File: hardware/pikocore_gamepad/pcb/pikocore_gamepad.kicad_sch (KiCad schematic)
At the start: 91 parts, among them J1 PHONES, J2 MIDI OUT, J3 MIDI IN, J4 ST7789_240x240, J5 SPEAKER 8R, J6 microSD, J7 EXP, SW1 DPAD_UP, SW10 BTN_R, SW11 BTN_START, SW12 BTN_SELECT, SW13 NAV1, SW14 NAV2, SW15 PWR, SW2 DPAD_DOWN, SW3 DPAD_LEFT, SW4 DPAD_RIGHT, SW5 BTN_X, SW6 BTN_Y, SW7 BTN_A, SW8 BTN_B, SW9 BTN_L, U1 RP2350-Plus-16MB, U10 PCF8574MT, U11 PCF8574MT, U12 PCF8574MT, U2 TPS61023DRLR, U3 NJM4556AD, U4 PAM8302A, U5 PCM5102APWR, U6 H11L1

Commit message: hw: pikocore_gamepad schematic — checks green, ERC clean
Regenerates the schematic (gen_sch.py), exports the netlist, generates the
placement-only PCB (gen_pcb.py), runs checks/run_all.py and kicad-cli sch erc
as end-to-end verification for the pikocore_gamepad PCB fork.

- checks/run_all.py: G-5 (dup refs), G-4 (pinmap vs firmware, 23/23), G-2
  (netlist match, 226/226), placement (no overlaps) all pass. G-0 still
  reports the 7 pre-existing provisional constants + 4 provisional
  footprints inherited from GAMESETUP (TPS61023/JACK_AUDIO pinouts,
  BOOST_*, BTN_FP/BTN_RA_FP/OPAMP_FP/JACK_FP, LCD_PIN_ROW_Y/LCD_HOLE_INSET,
  BOARD_W/BOARD_H) — expected, not resolved by this plan.
- kicad-cli sch erc: 0 errors, 65 warnings. 3 are the expected dangling
  EXP_GP26/27/28 labels. The other 62 are lib_symbol_issues warnings caused
  by a pre-existing mismatch between sym-lib-table's unrenamed 'gamesetup'
  nickname and gen_sch.py's PROJECT="pikocore_gamepad" lib_id prefix — see
  gen_sch.py's own comment referencing a not-yet-existing 'Task 8' to fix
  sym-lib-table. Flagged for follow-up, not fixed here (out of scope).

logs/erc.log is force-added since pcb/.gitignore's 'logs/*' rule would
otherwise exclude it, per this task's explicit instruction to commit it as
evidence. kicad_pcb/.net are committed to match GAMESETUP's own convention
of tracking these (verified via git ls-files in C:/midigame/GAMESETUP).

Co-Authored-By: Claude Sonnet 5 <noreply@anthropic.com>
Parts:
- removed C1, C10, C11, C13, C15, C2, C20, C27, C29, C3, C30, C7: 100nF, Capacitor_SMD:C_0603_1608Metric, symbol gamesetup:C
- removed C12, C14, C16, C28, C31: 10uF, Capacitor_SMD:CP_Elec_6.3x5.4, symbol gamesetup:CP
- removed C17, C18: 2n2, Capacitor_SMD:C_0603_1608Metric, symbol gamesetup:C
- removed C19, C6: 100uF, Capacitor_SMD:CP_Elec_6.3x5.4, symbol gamesetup:CP
- removed C21, C22, C25, C26: 1uF, Capacitor_SMD:C_0603_1608Metric, symbol gamesetup:C
- removed C23, C24: 470uF, Capacitor_SMD:CP_Elec_6.3x5.4, symbol gamesetup:CP
- removed C4: 10uF, Capacitor_SMD:C_0603_1608Metric, symbol gamesetup:C
- removed C5: 22uF, Capacitor_SMD:C_0603_1608Metric, symbol gamesetup:C
- removed C8, C9: 2u2, Capacitor_SMD:C_0603_1608Metric, symbol gamesetup:C
- removed D1: 1N4148W, Diode_SMD:D_SOD-123, symbol gamesetup:D
- removed J1: PHONES, Connector_PinHeader_2.54mm:PinHeader_1x04_P2.54mm_Vertical, symbol gamesetup:JACK_AUDIO
- removed J2: MIDI OUT, Connector_PinHeader_2.54mm:PinHeader_1x03_P2.54mm_Vertical, symbol gamesetup:JACK_TRS
- removed J3: MIDI IN, Connector_PinHeader_2.54mm:PinHeader_1x03_P2.54mm_Vertical, symbol gamesetup:JACK_TRS
- removed J5: SPEAKER 8R, Connector_JST:JST_PH_B2B-PH-K_1x02_P2.00mm_Vertical, symbol gamesetup:Conn_01x02
- removed J6: microSD, Connector_PinHeader_2.54mm:PinHeader_1x08_P2.54mm_Vertical, symbol gamesetup:MICROSD
- removed J7: EXP, Connector_PinHeader_2.54mm:PinHeader_1x09_P2.54mm_Vertical, symbol gamesetup:Conn_01x09
- removed L1, L2: 2u2, Inductor_SMD:L_1210_3225Metric, symbol gamesetup:L
- removed R1, R2: 4.7k, Resistor_SMD:R_0603_1608Metric, symbol gamesetup:R
- removed R10, R12, R14, R15, R16, R17, R22, R23, R24, R3, R9: 10k, Resistor_SMD:R_0603_1608Metric, symbol gamesetup:R
- removed R11, R13: 20k, Resistor_SMD:R_0603_1608Metric, symbol gamesetup:R
- removed R18, R19: 33R, Resistor_SMD:R_0603_1608Metric, symbol gamesetup:R
- removed R20: 220R, Resistor_SMD:R_0603_1608Metric, symbol gamesetup:R
- removed R21: 1k, Resistor_SMD:R_0603_1608Metric, symbol gamesetup:R
- removed R4: 1M, Resistor_SMD:R_0603_1608Metric, symbol gamesetup:R
- removed R5: 200k, Resistor_SMD:R_0603_1608Metric, symbol gamesetup:R
- removed R6: 100k, Resistor_SMD:R_0603_1608Metric, symbol gamesetup:R
- removed R7, R8: 470R, Resistor_SMD:R_0603_1608Metric, symbol gamesetup:R
- removed SW1: DPAD_UP, gamesetup_lcsc:SW-TH_4P-L4.5-W4.5-P3.00-LS5.5, symbol gamesetup:SW_Push
- removed SW11: BTN_START, gamesetup_lcsc:SW-TH_4P-L4.5-W4.5-P3.00-LS5.5, symbol gamesetup:SW_Push
- removed SW12: BTN_SELECT, gamesetup_lcsc:SW-TH_4P-L4.5-W4.5-P3.00-LS5.5, symbol gamesetup:SW_Push
- removed SW14: NAV2, gamesetup_lcsc:SW-TH_WS-1004-ARL10026, symbol gamesetup:NAV_WS1004
- removed SW15: PWR, gamesetup_lcsc:SW-TH_SK12D07VG3, symbol gamesetup:SK12D07
- removed SW3: DPAD_LEFT, gamesetup_lcsc:SW-TH_4P-L4.5-W4.5-P3.00-LS5.5, symbol gamesetup:SW_Push
- removed SW4: DPAD_RIGHT, gamesetup_lcsc:SW-TH_4P-L4.5-W4.5-P3.00-LS5.5, symbol gamesetup:SW_Push
- removed SW6: BTN_Y, gamesetup_lcsc:SW-TH_4P-L4.5-W4.5-P3.00-LS5.5, symbol gamesetup:SW_Push
- removed SW7: BTN_A, gamesetup_lcsc:SW-TH_4P-L4.5-W4.5-P3.00-LS5.5, symbol gamesetup:SW_Push
- removed SW8: BTN_B, gamesetup_lcsc:SW-TH_4P-L4.5-W4.5-P3.00-LS5.5, symbol gamesetup:SW_Push
- removed TP2: SPARE2, TestPoint:TestPoint_Pad_D1.5mm, symbol gamesetup:TP
- removed U11, U12: PCF8574MT, Package_SO:TSSOP-16_4.4x5mm_P0.65mm, symbol gamesetup:PCF8574
- removed U2: TPS61023DRLR, Package_TO_SOT_SMD:SOT-563, symbol gamesetup:TPS61023
- removed U3: NJM4556AD, Package_SO:SOIC-8_3.9x4.9mm_P1.27mm, symbol gamesetup:NJM4556AD
- removed U4: PAM8302A, gamesetup_lcsc:MSOP-8_L3.0-W3.0-P0.65-LS5.0-BL, symbol gamesetup:PAM8302A
- removed U5: PCM5102APWR, gamesetup_lcsc:TSSOP-20_L6.5-W4.4-P0.65-LS6.4-BL, symbol gamesetup:PCM5102A
- removed U6: H11L1, Package_SO:SO-6_4.4x3.6mm_P1.27mm, symbol gamesetup:H11L1
- added C10, C15, C20, C27, C7: 100nF, Capacitor_SMD:C_0603_1608Metric, symbol pikocore_gamepad:C
- added C14, C16, C28: 10uF, Capacitor_SMD:CP_Elec_6.3x5.4, symbol pikocore_gamepad:CP
- added C17, C18: 2n2, Capacitor_SMD:C_0603_1608Metric, symbol pikocore_gamepad:C
- added C19, C6: 100uF, Capacitor_SMD:CP_Elec_6.3x5.4, symbol pikocore_gamepad:CP
- added C21, C22, C25, C26: 1uF, Capacitor_SMD:C_0603_1608Metric, symbol pikocore_gamepad:C
- added C23, C24: 470uF, Capacitor_SMD:CP_Elec_6.3x5.4, symbol pikocore_gamepad:CP
- added C4: 10uF, Capacitor_SMD:C_0603_1608Metric, symbol pikocore_gamepad:C
- added C5: 22uF, Capacitor_SMD:C_0603_1608Metric, symbol pikocore_gamepad:C
- added C8, C9: 2u2, Capacitor_SMD:C_0603_1608Metric, symbol pikocore_gamepad:C
- added J1: PHONES, Connector_PinHeader_2.54mm:PinHeader_1x04_P2.54mm_Vertical, symbol pikocore_gamepad:JACK_AUDIO
- added J5: SPEAKER 8R, Connector_JST:JST_PH_B2B-PH-K_1x02_P2.00mm_Vertical, symbol pikocore_gamepad:Conn_01x02
- added L1: 2u2, Inductor_SMD:L_1210_3225Metric, symbol pikocore_gamepad:L
- added R10, R12, R14, R15, R16, R17, R9: 10k, Resistor_SMD:R_0603_1608Metric, symbol pikocore_gamepad:R
- added R11, R13: 20k, Resistor_SMD:R_0603_1608Metric, symbol pikocore_gamepad:R
- added R5: 200k, Resistor_SMD:R_0603_1608Metric, symbol pikocore_gamepad:R
- added R6: 100k, Resistor_SMD:R_0603_1608Metric, symbol pikocore_gamepad:R
- added R7, R8: 470R, Resistor_SMD:R_0603_1608Metric, symbol pikocore_gamepad:R
- added SW10: BTN_R, Button_Switch_THT:SW_Tactile_SPST_Angled_PTS645Vx39-2LFS, symbol pikocore_gamepad:SW_Push_RA
- added SW11: BTN_START, gamesetup_lcsc:SW-TH_4P-L4.5-W4.5-P3.00-LS5.5, symbol pikocore_gamepad:SW_Push
- added SW12: BTN_SELECT, gamesetup_lcsc:SW-TH_4P-L4.5-W4.5-P3.00-LS5.5, symbol pikocore_gamepad:SW_Push
- added SW15: PWR, gamesetup_lcsc:SW-TH_SK12D07VG3, symbol pikocore_gamepad:SK12D07
- added SW2: DPAD_DOWN, gamesetup_lcsc:SW-TH_4P-L4.5-W4.5-P3.00-LS5.5, symbol pikocore_gamepad:SW_Push
- added SW3: DPAD_LEFT, gamesetup_lcsc:SW-TH_4P-L4.5-W4.5-P3.00-LS5.5, symbol pikocore_gamepad:SW_Push
- added SW4: DPAD_RIGHT, gamesetup_lcsc:SW-TH_4P-L4.5-W4.5-P3.00-LS5.5, symbol pikocore_gamepad:SW_Push
- added SW5: BTN_X, gamesetup_lcsc:SW-TH_4P-L4.5-W4.5-P3.00-LS5.5, symbol pikocore_gamepad:SW_Push
- added SW6: BTN_Y, gamesetup_lcsc:SW-TH_4P-L4.5-W4.5-P3.00-LS5.5, symbol pikocore_gamepad:SW_Push
- added SW7: BTN_A, gamesetup_lcsc:SW-TH_4P-L4.5-W4.5-P3.00-LS5.5, symbol pikocore_gamepad:SW_Push
- added SW8: BTN_B, gamesetup_lcsc:SW-TH_4P-L4.5-W4.5-P3.00-LS5.5, symbol pikocore_gamepad:SW_Push
- added SW9: BTN_L, Button_Switch_THT:SW_Tactile_SPST_Angled_PTS645Vx39-2LFS, symbol pikocore_gamepad:SW_Push_RA
- added U2: TPS61023DRLR, Package_TO_SOT_SMD:SOT-563, symbol pikocore_gamepad:TPS61023
- added U3: NJM4556AD, Package_SO:SOIC-8_3.9x4.9mm_P1.27mm, symbol pikocore_gamepad:NJM4556AD
- added U4: PAM8302A, gamesetup_lcsc:MSOP-8_L3.0-W3.0-P0.65-LS5.0-BL, symbol pikocore_gamepad:PAM8302A
- C11: renamed from SW9; value BTN_L -> 100nF; footprint Button_Switch_THT:SW_Tactile_SPST_Angled_PTS645Vx39-2LFS -> Capacitor_SMD:C_0603_1608Metric; symbol gamesetup:SW_Push_RA -> pikocore_gamepad:C
- C12: renamed from SW10; value BTN_R -> 10uF; footprint Button_Switch_THT:SW_Tactile_SPST_Angled_PTS645Vx39-2LFS -> Capacitor_SMD:CP_Elec_6.3x5.4; symbol gamesetup:SW_Push_RA -> pikocore_gamepad:CP
- C13: renamed from SW13; value NAV1 -> 100nF; footprint gamesetup_lcsc:SW-TH_WS-1004-ARL10026 -> Capacitor_SMD:C_0603_1608Metric; symbol gamesetup:NAV_WS1004 -> pikocore_gamepad:C; LCSC C42377836 -> (none)
- J4: symbol gamesetup:LCD_ST7789 -> pikocore_gamepad:LCD_ST7789
- L2: renamed from TP1; value SPARE1 -> 2u2; footprint TestPoint:TestPoint_Pad_D1.5mm -> Inductor_SMD:L_1210_3225Metric; symbol gamesetup:TP -> pikocore_gamepad:L; LCSC (none) -> C3002559
- R4: renamed from SW2; value DPAD_DOWN -> 1M; footprint gamesetup_lcsc:SW-TH_4P-L4.5-W4.5-P3.00-LS5.5 -> Resistor_SMD:R_0603_1608Metric; symbol gamesetup:SW_Push -> pikocore_gamepad:R
- SW1: renamed from U10; value PCF8574MT -> DPAD_UP; footprint Package_SO:TSSOP-16_4.4x5mm_P0.65mm -> gamesetup_lcsc:SW-TH_4P-L4.5-W4.5-P3.00-LS5.5; symbol gamesetup:PCF8574 -> pikocore_gamepad:SW_Push; LCSC C22461594 -> (none)
- U1: symbol gamesetup:RP2350-Plus -> pikocore_gamepad:RP2350-Plus
- U5: renamed from SW5; value BTN_X -> PCM5102APWR; footprint gamesetup_lcsc:SW-TH_4P-L4.5-W4.5-P3.00-LS5.5 -> gamesetup_lcsc:TSSOP-20_L6.5-W4.4-P0.65-LS6.4-BL; symbol gamesetup:SW_Push -> pikocore_gamepad:PCM5102A; LCSC (none) -> C107671
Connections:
- net EXP_GP14 is gone; now on net BTN_START: U1.19 (GP14)
- net EXP_GP15 is gone; now on net BTN_SELECT: U1.20 (GP15)
- net EXP_GP9 is gone; now on net DPAD_RIGHT: U1.12 (GP9)
- net MIDI_RX is gone; now on net DPAD_DOWN: U1.2 (GP1)
- net MIDI_TX is gone; now on net DPAD_UP: U1.1 (GP0)
- net NAV1_LEFT is gone; now on net GND: C13.2
- net SD_CS is gone; now on net BTN_B: U1.17 (GP13)
- net SD_MISO is gone; now on net BTN_A: U1.16 (GP12)
- net SD_MOSI is gone; now on net BTN_Y: U1.15 (GP11)
- net SD_SCK is gone; now on net BTN_X: U1.14 (GP10)
- net TP_SPARE1 is gone; now on net VSYS: L2.1
- net 3V3: now also C11.1, C12.1 (+), C13.1, U5.1 (CPVDD), U5.20 (DVDD), U5.8 (AVDD), C14.1 (+), C15.1, C16.1 (+), R15.1; no longer SW1.16 (VDD)
- net 5V: now also R4.1, C5.1, C6.1 (+), C7.1, R9.1, U2.5 (VOUT), U3.8 (V+)
- net AOUT_L: now also C17.1, C21.1, R7.2
- net AOUT_R: now also C18.1, C22.1, R8.2
- net AUDIO_L: now also C23.1 (+), R12.2, R16.1, U3.1 (OUTA)
- net AUDIO_R: now also C24.1 (+), R14.2, R17.1, U3.7 (OUTB)
- net BOOST_FB: now also R4.2, R5.1, U2.4 (FB)
- net BOOST_SW: now also L1.2, U2.6 (SW)
- net BTN_A: now also SW7.1 (A); no longer SW1.11 (P6)
- net BTN_B: now also SW8.1 (A); no longer SW1.12 (P7)
- net BTN_L: now also U1.24 (GP18), SW9.1 (A); no longer C11.1 (A)
- net BTN_R: now also U1.25 (GP19), SW10.1 (A); no longer C12.1 (A)
- net BTN_SELECT: now also SW12.1 (A)
- net BTN_START: now also SW11.1 (A)
- net BTN_X: now also SW5.1 (A); no longer SW1.9 (P4), U5.1 (A)
- net BTN_Y: now also SW6.1 (A); no longer SW1.10 (P5)
- net CAPM: now also U5.4 (CAPM), C8.2
- net CAPP: now also U5.2 (CAPP), C8.1
- net DACOUT_L: now also U5.6 (OUTL), R7.1
- net DACOUT_R: now also U5.7 (OUTR), R8.1
- net DAC_XSMT: now also U5.17 (XSMT), R6.1
- net DPAD_DOWN: now also SW2.1 (A); no longer R4.1 (A), SW1.5 (P1)
- net DPAD_LEFT: now also U1.6 (GP4), SW3.1 (A); no longer SW1.6 (P2)
- net DPAD_RIGHT: now also SW4.1 (A); no longer SW1.7 (P3)
- net DPAD_UP: now also SW1.1 (A); no longer SW1.4 (P0)
- net GND: now also SW1.4 (B), U5.10 (DEMP), U5.11 (FLT), U5.12 (SCK), U5.16 (FMT), U5.19 (DGND), U5.3 (CPGND), U5.9 (AGND), C10.2, C14.2 (-), C15.2, C16.2 (-), C17.2, C18.2, C19.2 (-), C20.2, C26.2, C27.2, C28.2 (-), C4.2, C5.2, C6.2 (-), C7.2, C9.2, J1.3 (SLEEVE), R10.2, R5.2, R6.2, SW10.2 (B), SW11.4 (B), SW12.4 (B), SW15.1 (A), SW15.4 (MNT), SW15.5 (MNT), SW2.4 (B), SW3.4 (B), SW4.4 (B), SW5.4 (B), SW6.4 (B), SW7.4 (B), SW8.4 (B), SW9.2 (B), U2.2 (GND), U3.4 (V-), U4.7 (GND); no longer C13.1 (COM), R4.4 (B), SW1.1 (A0), SW1.2 (A1), SW1.3 (A2), SW1.8 (VSS), U5.4 (B)
- net I2S_BCK: now also U5.13 (BCK)
- net I2S_DIN: now also U5.14 (DIN)
- net I2S_LRCK: now also U5.15 (LRCK)
- net INL: now also C21.2, R11.1
- net INR: now also C22.2, R13.1
- net JACK_DET: now also J1.4 (DET), R15.2
- net JACK_L: now also C23.2 (-), J1.1 (TIP)
- net JACK_R: now also C24.2 (-), J1.2 (RING)
- net LDOO: now also U5.18 (LDOO), C10.1
- net OPL_N: now also R11.2, R12.1, U3.2 (INA-)
- net OPR_N: now also R13.2, R14.1, U3.6 (INB-)
- net PWR_EN: now also SW15.2 (COM)
- net SPK_INN: now also C26.1, U4.4 (IN-)
- net SPK_INP: now also C25.2, U4.3 (IN+)
- net SPK_N: now also J5.2, U4.8 (VO-)
- net SPK_P: now also J5.1, U4.5 (VO+)
- net SPK_SHDN: now also U4.1 (SD)
- net SPK_SUM: now also C25.1, R16.2, R17.2
- net VNEG: now also U5.5 (VNEG), C9.1
- net VREF25: now also C19.1 (+), C20.1, R10.1, R9.2, U3.3 (INA+), U3.5 (INB+)
- net VSYS: now also C27.1, C28.1 (+), U4.6 (VDD)
- net VSYS_F: now also L2.2, C4.1, L1.1, U2.1 (VIN), U2.3 (EN)
- removed net I2C_SCL: SW1.14 (SCL), U1.25 (GP19)
- removed net I2C_SDA: SW1.15 (SDA), U1.24 (GP18)
- removed net NAV1_CENTER: C13.3 (CENTER)
- removed net NAV1_DOWN: C13.6 (DOWN)
- removed net NAV1_RIGHT: C13.5 (RIGHT)
- removed net NAV1_UP: C13.4 (UP)
- removed net PCF_INT: SW1.13 (INT), U1.6 (GP4)
- no-connect marks 26 -> 25
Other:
- note added: "ENTRADA: los 12 botones van directo a GPIO del modulo (sin expansor I2C) — ver pinmap.py para la asignacion."
- note added: "VERIFICAR ANTES DE FABRICAR (correr checks/check_verified.py): - Cotas del modulo LCD que el drawing no acota: vertical de la fila de pines, y el offset de los agujeros (la cota dice 2.19 y la nota china 2.5). - Pinout de TPS61023 y del jack de audio: ninguno viene verificado de V1 y sus simbolos lo dicen. - Valores del lazo del boost (inductor y divisor de realimentacion). Los pinouts de PCM5102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"
- note added: "pikocore_gamepad - PCB panel unico, 4 capas. MCU Waveshare RP2350-Plus 16MB en socket 2x20. La bateria LiPo va al PH1.25 del propio modulo (cargador ETA6096 a bordo): la placa no lleva circuito de carga. SW15 apaga el rail 3V3 del modulo via 3V3_EN, que tiene pull-up interno de 100K a VSYS."
- note removed: "ENTRADA: los 22 contactos de switch (12 tacts + 2 nav de 5 vias) NO entran en los 26 GPIO que expone el modulo, asi que van por 3 expansores PCF8574 en I2C1 (0x20/0x21/0x22). Cada nav queda ENTERO en un solo chip: repartido entre dos, dos lecturas distintas podrian mostrar una diagonal que el usuario nunca hizo. Los 3 /INT van en wired-OR a GP4."
- note removed: "GAMESETUP V2 - PCB panel unico, 4 capas. MCU Waveshare RP2350-Plus 16MB en socket 2x20. La bateria LiPo va al PH1.25 del propio modulo (cargador ETA6096 a bordo): la placa no lleva circuito de carga. SW15 apaga el rail 3V3 del modulo via 3V3_EN, que tiene pull-up interno de 100K a VSYS."
- note removed: "VERIFICAR ANTES DE FABRICAR (correr checks/check_verified.py): - Cotas del modulo LCD que el drawing no acota: vertical de la fila de pines, y el offset de los agujeros (la cota dice 2.19 y la nota china 2.5). - Pinout de TPS61023, H11L1, los dos jacks TRS, el jack de audio y el socket microSD: ninguno viene verificado de V1 y sus simbolos lo dicen. - Valores del lazo del boost (inductor y diviso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"
- title: GAMESETUP V2 - panel principal -> pikocore_gamepad - panel principal
- moved on the sheet: C11, C12

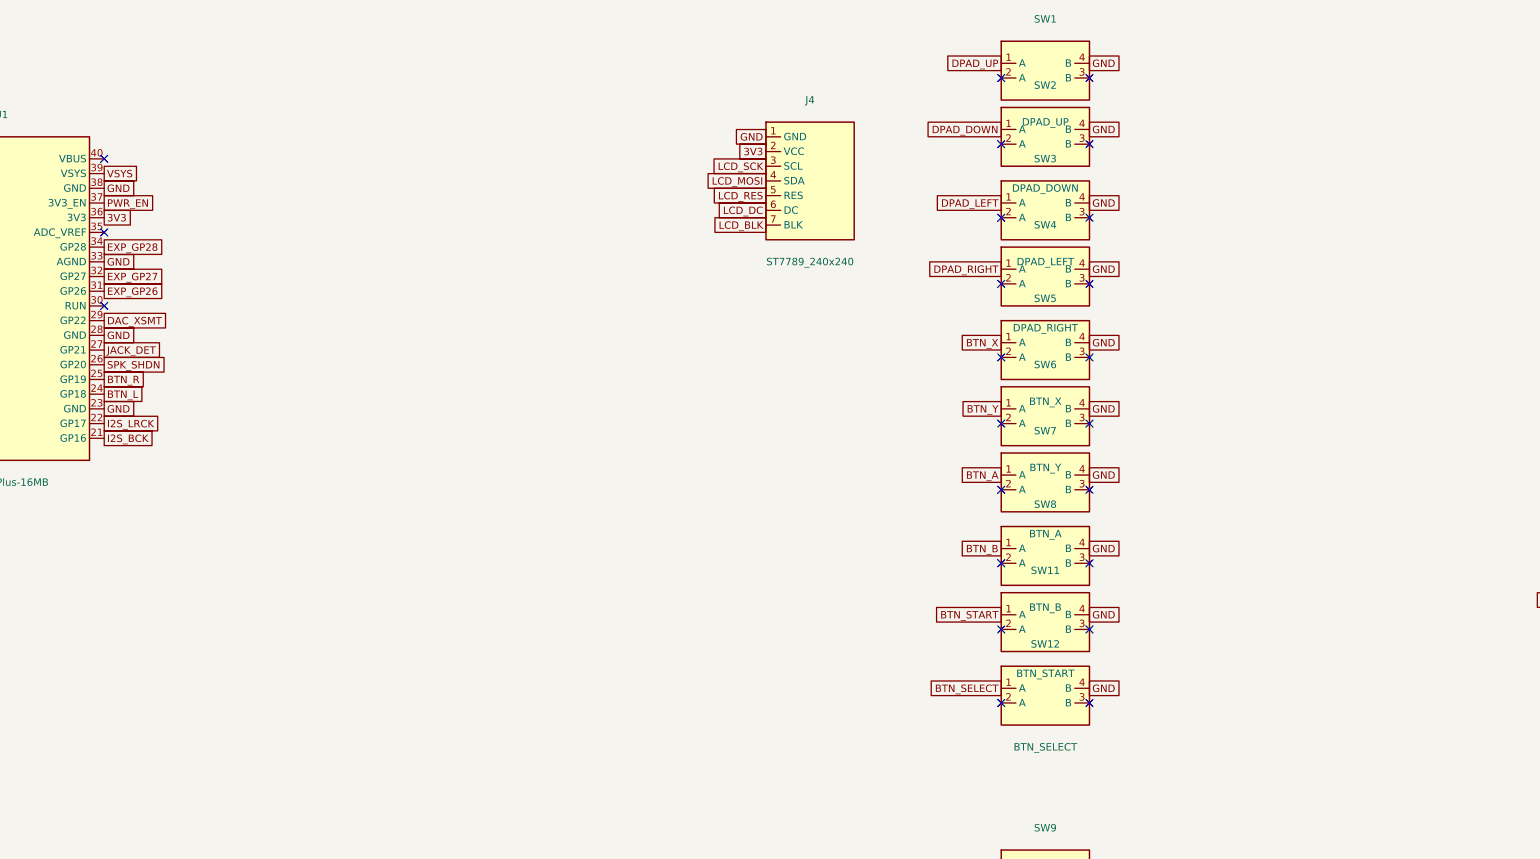
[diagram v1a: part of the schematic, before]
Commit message: hw: pikocore_gamepad schematic/PCB regenerated — NAV5 + speaker reloc, checks green
Co-Authored-By: Claude Sonnet 5 <noreply@anthropic.com>
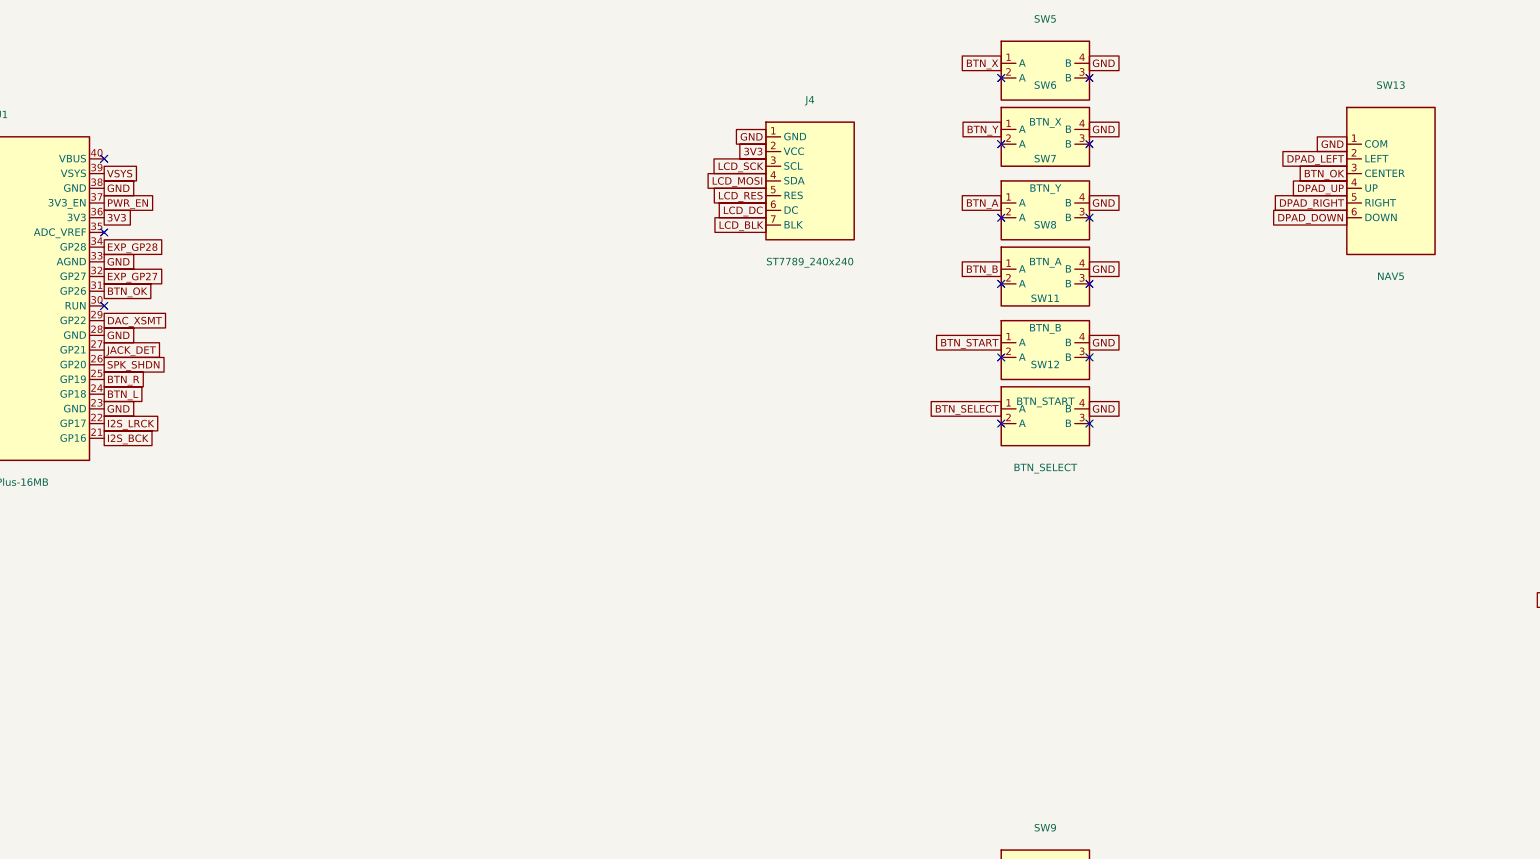
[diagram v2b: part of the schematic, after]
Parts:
- removed L1, L2: 2u2, Inductor_SMD:L_1210_3225Metric, symbol pikocore_gamepad:L
- removed SW11: BTN_START, gamesetup_lcsc:SW-TH_4P-L4.5-W4.5-P3.00-LS5.5, symbol pikocore_gamepad:SW_Push
- removed SW12: BTN_SELECT, gamesetup_lcsc:SW-TH_4P-L4.5-W4.5-P3.00-LS5.5, symbol pikocore_gamepad:SW_Push
- removed SW8: BTN_B, gamesetup_lcsc:SW-TH_4P-L4.5-W4.5-P3.00-LS5.5, symbol pikocore_gamepad:SW_Push
- removed SW9: BTN_L, Button_Switch_THT:SW_Tactile_SPST_Angled_PTS645Vx39-2LFS, symbol pikocore_gamepad:SW_Push_RA
- added SW13: NAV5, gamesetup_lcsc:SW-TH_WS-1004-ARL10026, symbol pikocore_gamepad:NAV_WS1004
- added SW15: PWR, gamesetup_lcsc:SW-TH_SK12D07VG3, symbol pikocore_gamepad:SK12D07
- added U2: TPS61023DRLR, Package_TO_SOT_SMD:SOT-563, symbol pikocore_gamepad:TPS61023
- L1: renamed from U2; value TPS61023DRLR -> 2u2; footprint Package_TO_SOT_SMD:SOT-563 -> Inductor_SMD:L_1210_3225Metric; symbol pikocore_gamepad:TPS61023 -> pikocore_gamepad:L; LCSC C919459 -> C3002559
- L2: renamed from SW15; value PWR -> 2u2; footprint gamesetup_lcsc:SW-TH_SK12D07VG3 -> Inductor_SMD:L_1210_3225Metric; symbol pikocore_gamepad:SK12D07 -> pikocore_gamepad:L; LCSC C431547 -> C3002559
- SW11: renamed from SW5; value BTN_X -> BTN_START
- SW12: renamed from SW6; value BTN_Y -> BTN_SELECT
- SW5: renamed from SW1; value DPAD_UP -> BTN_X
- SW6: renamed from SW2; value DPAD_DOWN -> BTN_Y
- SW7: renamed from SW3; value DPAD_LEFT -> BTN_A
- SW8: renamed from SW4; value DPAD_RIGHT -> BTN_B
- SW9: renamed from SW7; value BTN_A -> BTN_L; footprint gamesetup_lcsc:SW-TH_4P-L4.5-W4.5-P3.00-LS5.5 -> Button_Switch_THT:SW_Tactile_SPST_Angled_PTS645Vx39-2LFS; symbol pikocore_gamepad:SW_Push -> pikocore_gamepad:SW_Push_RA
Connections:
- net 5V: now also U2.5 (VOUT); no longer L1.5 (VOUT)
- net BOOST_FB: now also U2.4 (FB); no longer L1.4 (FB)
- net BOOST_SW: now also L1.2, U2.6 (SW); no longer L1.6 (SW)
- net BTN_A: now also SW7.1 (A); no longer SW9.1 (A)
- net BTN_B: now also SW8.1 (A)
- net BTN_L: now also SW9.1 (A)
- net BTN_SELECT: now also SW12.1 (A)
- net BTN_START: now also SW11.1 (A)
- net BTN_X: now also SW5.1 (A); no longer SW11.1 (A)
- net BTN_Y: now also SW6.1 (A); no longer SW12.1 (A)
- net DPAD_DOWN: now also SW13.6 (DOWN); no longer SW6.1 (A)
- net DPAD_LEFT: now also SW13.2 (LEFT); no longer SW7.1 (A)
- net DPAD_RIGHT: now also SW13.5 (RIGHT); no longer SW8.1 (A)
- net DPAD_UP: now also SW13.4 (UP); no longer SW5.1 (A)
- net GND: now also SW9.2 (B), SW13.1 (COM), SW15.1 (A), SW15.4 (MNT), SW15.5 (MNT), U2.2 (GND); no longer L1.2 (GND), L2.1 (A), L2.4 (MNT), L2.5 (MNT), SW9.4 (B)
- net PWR_EN: now also SW15.2 (COM); no longer L2.2 (COM)
- net VSYS: now also L2.1
- net VSYS_F: now also L2.2, U2.1 (VIN), U2.3 (EN); no longer L1.3 (EN)
- net EXP_GP26 renamed BTN_OK
- net BTN_OK: now also SW13.3 (CENTER)
- no-connect marks 25 -> 17
